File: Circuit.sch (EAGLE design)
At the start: 114 parts, among them IC1 LM1117T-3.3-V

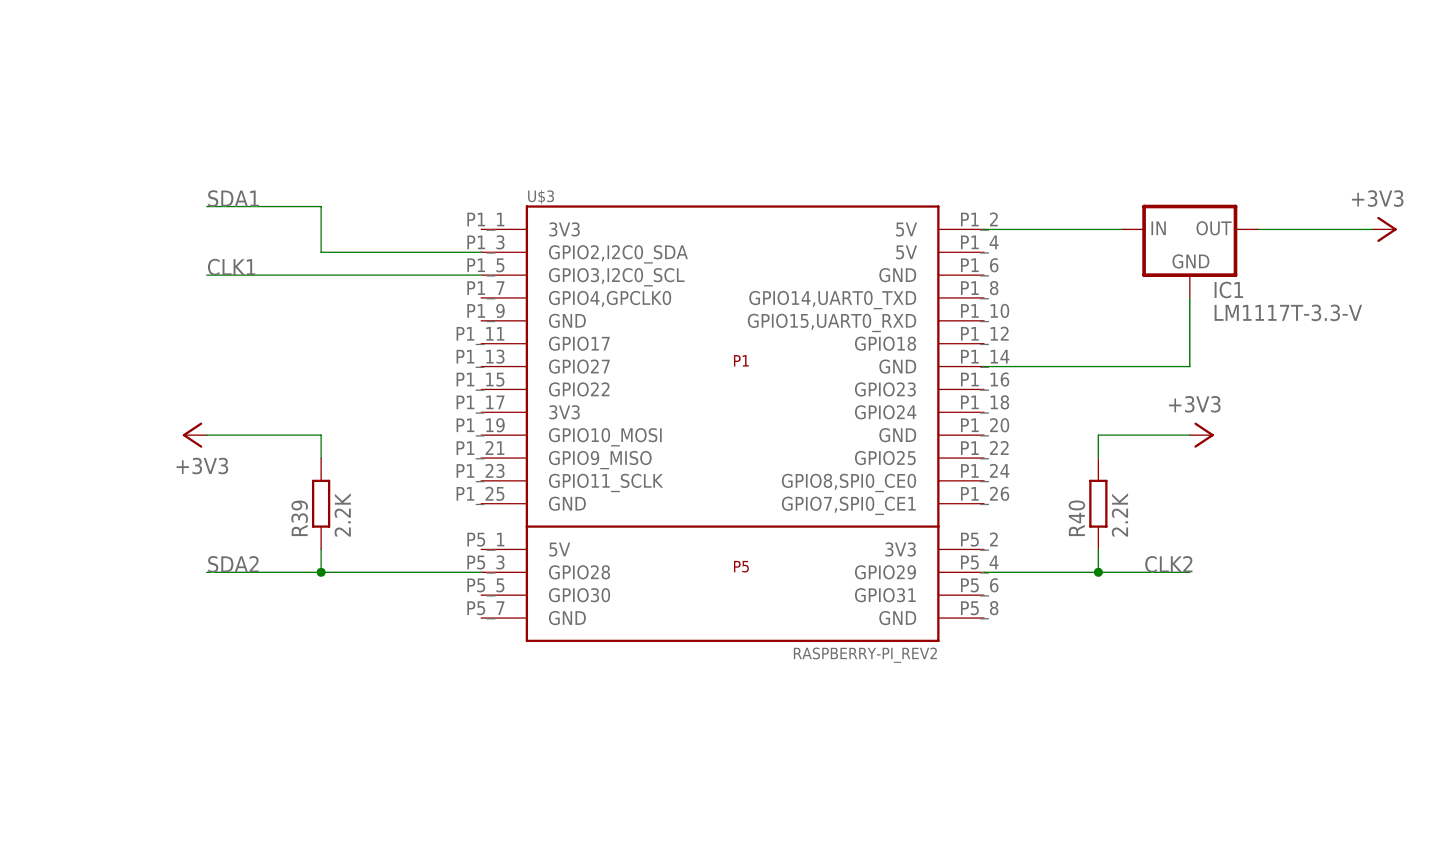
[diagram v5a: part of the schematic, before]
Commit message: Changed to smashed raspi headers
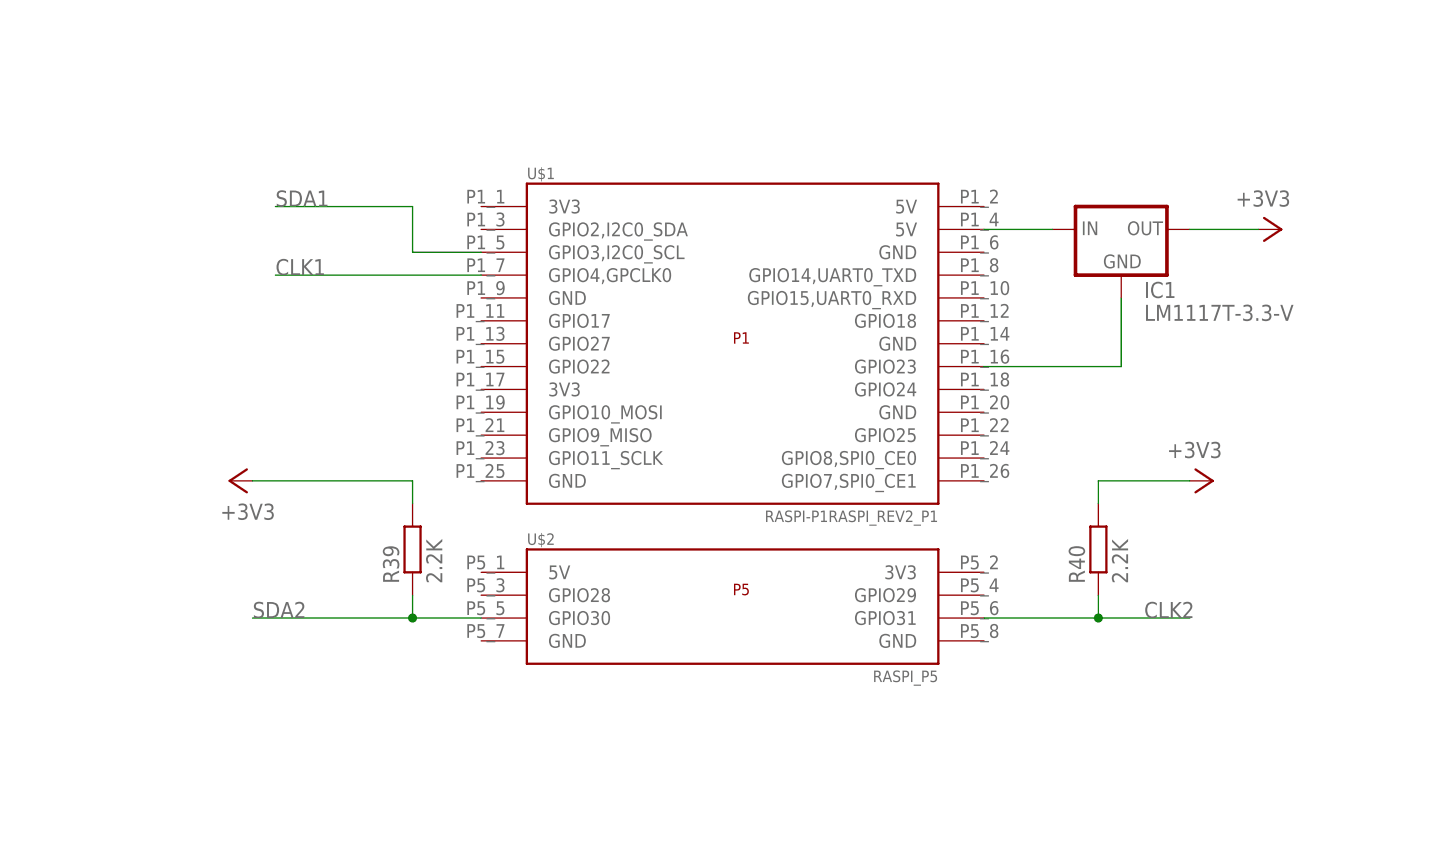
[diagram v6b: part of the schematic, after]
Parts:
- removed U$3: RASPBERRY-PI_REV2, RaspberryPi:RASPBERRY-PI_REV2
- added U$1: RASPI-P1RASPI_REV2_P1, Gyros:RASPI-P1RASPI_REV2_P1
- added U$2: RASPI_P5, RaspberryPi:RASPI_P5
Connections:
- net CLK1: now also U$1.GPIO4,GPCLK0; no longer U$3.GPIO3,I2C0_SCL
- net CLK2: now also U$2.GPIO31; no longer U$3.GPIO29
- net GND: now also U$1.GPIO23; no longer U$3.GND@14
- net N$10: now also U$1.5V@4; no longer U$3.5V@2
- net SDA1: now also U$1.GPIO3,I2C0_SCL; no longer U$3.GPIO2,I2C0_SDA
- net SDA2: now also U$2.GPIO30; no longer U$3.GPIO28
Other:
- moved on the sheet: IC1, R39, R40
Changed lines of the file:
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@@
 </classes>
 <parts>
-<part name="U$3" library="RaspberryPi" deviceset="RASPBERRY-PI_REV2" device=""/>
 <part name="MPU1" library="Gyros" deviceset="MPU-3300" device=""/>
 <part name="ITG1" library="Gyros" deviceset="ITG-3050" device=""/>
@@
 <part name="+3V51" library="supply1" deviceset="+3V3" device=""/>
 <part name="+3V31" library="supply1" deviceset="+3V3" device=""/>
+<part name="U$1" library="Gyros" deviceset="RASPI-P1" device="RASPI_REV2_P1"/>
+<part name="U$2" library="RaspberryPi" deviceset="RASPI_P5" device=""/>
 </parts>
 <sheets>
@@
 </plain>
 <instances>
-<instance part="U$3" gate="G$1" x="421.64" y="177.8"/>
 <instance part="MPU1" gate="G$1" x="-58.42" y="317.5"/>
 <instance part="ITG1" gate="G$1" x="-50.8" y="226.06"/>
@@
 <instance part="R9" gate="G$1" x="-22.86" y="345.44" rot="R180"/>
 <instance part="+3V46" gate="G$1" x="-5.08" y="350.52" rot="R270"/>
-<instance part="IC1" gate="G$1" x="472.44" y="193.04"/>
-<instance part="+3V5" gate="G$1" x="495.3" y="193.04" rot="R270"/>
-<instance part="R39" gate="G$1" x="375.92" y="162.56" rot="R90"/>
-<instance part="R40" gate="G$1" x="462.28" y="162.56" rot="R90"/>
-<instance part="+3V47" gate="G$1" x="474.98" y="170.18" rot="R270"/>
-<instance part="+3V48" gate="G$1" x="360.68" y="170.18" rot="R90"/>
+<instance part="IC1" gate="G$1" x="464.82" y="193.04"/>
+<instance part="+3V5" gate="G$1" x="482.6" y="193.04" rot="R270"/>
+<instance part="R39" gate="G$1" x="386.08" y="157.48" rot="R90"/>
+<instance part="R40" gate="G$1" x="462.28" y="157.48" rot="R90"/>
+<instance part="+3V47" gate="G$1" x="474.98" y="165.1" rot="R270"/>
+<instance part="+3V48" gate="G$1" x="365.76" y="165.1" rot="R90"/>
 <instance part="R23" gate="G$1" x="198.12" y="350.52" rot="R180"/>
 <instance part="R28" gate="G$1" x="215.9" y="345.44" rot="R180"/>
@@
 <instance part="+3V51" gate="G$1" x="246.38" y="160.02" rot="R270"/>
 <instance part="+3V31" gate="G$1" x="208.28" y="119.38" rot="R270"/>
+<instance part="U$1" gate="G$1" x="421.64" y="180.34"/>
+<instance part="U$2" gate="G$1" x="421.64" y="152.4"/>
 </instances>
 <busses>
@@
 <segment>
 <pinref part="IC1" gate="G$1" pin="GND"/>
-<wire x1="472.44" y1="185.42" x2="472.44" y2="177.8" width="0.1524" layer="91"/>
-<pinref part="U$3" gate="G$1" pin="GND@14"/>
-<wire x1="472.44" y1="177.8" x2="449.58" y2="177.8" width="0.1524" layer="91"/>
+<wire x1="464.82" y1="185.42" x2="464.82" y2="177.8" width="0.1524" layer="91"/>
+<wire x1="464.82" y1="177.8" x2="449.58" y2="177.8" width="0.1524" layer="91"/>
+<pinref part="U$1" gate="G$1" pin="GPIO23"/>
 </segment>
 </net>
 <net name="CLK1" class="0">
 <segment>
-<pinref part="U$3" gate="G$1" pin="GPIO3,I2C0_SCL"/>
-<wire x1="393.7" y1="187.96" x2="363.22" y2="187.96" width="0.1524" layer="91"/>
-<label x="363.22" y="187.96" size="1.778" layer="95"/>
+<wire x1="393.7" y1="187.96" x2="370.84" y2="187.96" width="0.1524" layer="91"/>
+<label x="370.84" y="187.96" size="1.778" layer="95"/>
+<pinref part="U$1" gate="G$1" pin="GPIO4,GPCLK0"/>
 </segment>
 <segment>
@@
 <net name="SDA1" class="0">
 <segment>
-<pinref part="U$3" gate="G$1" pin="GPIO2,I2C0_SDA"/>
-<wire x1="393.7" y1="190.5" x2="375.92" y2="190.5" width="0.1524" layer="91"/>
-<wire x1="375.92" y1="190.5" x2="375.92" y2="195.58" width="0.1524" layer="91"/>
-<wire x1="375.92" y1="195.58" x2="363.22" y2="195.58" width="0.1524" layer="91"/>
-<label x="363.22" y="195.58" size="1.778" layer="95"/>
+<wire x1="393.7" y1="190.5" x2="386.08" y2="190.5" width="0.1524" layer="91"/>
+<wire x1="386.08" y1="190.5" x2="386.08" y2="195.58" width="0.1524" layer="91"/>
+<wire x1="386.08" y1="195.58" x2="370.84" y2="195.58" width="0.1524" layer="91"/>
+<label x="370.84" y="195.58" size="1.778" layer="95"/>
+<pinref part="U$1" gate="G$1" pin="GPIO3,I2C0_SCL"/>
 </segment>
 <segment>
@@
 <net name="SDA2" class="0">
 <segment>
-<pinref part="U$3" gate="G$1" pin="GPIO28"/>
-<wire x1="393.7" y1="154.94" x2="375.92" y2="154.94" width="0.1524" layer="91"/>
-<label x="363.22" y="154.94" size="1.778" layer="95"/>
+<wire x1="393.7" y1="149.86" x2="386.08" y2="149.86" width="0.1524" layer="91"/>
+<label x="368.3" y="149.86" size="1.778" layer="95"/>
 <pinref part="R39" gate="G$1" pin="1"/>
-<wire x1="375.92" y1="154.94" x2="363.22" y2="154.94" width="0.1524" layer="91"/>
-<wire x1="375.92" y1="154.94" x2="375.92" y2="157.48" width="0.1524" layer="91"/>
-<junction x="375.92" y="154.94"/>
+<wire x1="386.08" y1="149.86" x2="368.3" y2="149.86" width="0.1524" layer="91"/>
+<wire x1="386.08" y1="149.86" x2="386.08" y2="152.4" width="0.1524" layer="91"/>
+<junction x="386.08" y="149.86"/>
+<pinref part="U$2" gate="G$1" pin="GPIO30"/>
 </segment>
 <segment>
@@
 <segment>
 <pinref part="IC1" gate="G$1" pin="OUT"/>
-<wire x1="480.06" y1="193.04" x2="492.76" y2="193.04" width="0.1524" layer="91"/>
+<wire x1="472.44" y1="193.04" x2="480.06" y2="193.04" width="0.1524" layer="91"/>
 <pinref part="+3V5" gate="G$1" pin="+3V3"/>
 </segment>
 <segment>
 <pinref part="R40" gate="G$1" pin="2"/>
-<wire x1="462.28" y1="167.64" x2="462.28" y2="170.18" width="0.1524" layer="91"/>
-<wire x1="462.28" y1="170.18" x2="472.44" y2="170.18" width="0.1524" layer="91"/>
+<wire x1="462.28" y1="162.56" x2="462.28" y2="165.1" width="0.1524" layer="91"/>
+<wire x1="462.28" y1="165.1" x2="472.44" y2="165.1" width="0.1524" layer="91"/>
 <pinref part="+3V47" gate="G$1" pin="+3V3"/>
 </segment>
 <segment>
 <pinref part="R39" gate="G$1" pin="2"/>
-<wire x1="375.92" y1="167.64" x2="375.92" y2="170.18" width="0.1524" layer="91"/>
-<wire x1="375.92" y1="170.18" x2="363.22" y2="170.18" width="0.1524" layer="91"/>
+<wire x1="386.08" y1="162.56" x2="386.08" y2="165.1" width="0.1524" layer="91"/>
+<wire x1="386.08" y1="165.1" x2="368.3" y2="165.1" width="0.1524" layer="91"/>
 <pinref part="+3V48" gate="G$1" pin="+3V3"/>
 </segment>
@@
 </segment>
 <segment>
-<pinref part="U$3" gate="G$1" pin="GPIO29"/>
-<wire x1="449.58" y1="154.94" x2="462.28" y2="154.94" width="0.1524" layer="91"/>
-<label x="467.36" y="154.94" size="1.778" layer="95"/>
+<wire x1="449.58" y1="149.86" x2="462.28" y2="149.86" width="0.1524" layer="91"/>
+<label x="467.36" y="149.86" size="1.778" layer="95"/>
 <pinref part="R40" gate="G$1" pin="1"/>
-<wire x1="462.28" y1="154.94" x2="472.44" y2="154.94" width="0.1524" layer="91"/>
-<wire x1="462.28" y1="154.94" x2="462.28" y2="157.48" width="0.1524" layer="91"/>
-<junction x="462.28" y="154.94"/>
+<wire x1="462.28" y1="149.86" x2="472.44" y2="149.86" width="0.1524" layer="91"/>
+<wire x1="462.28" y1="149.86" x2="462.28" y2="152.4" width="0.1524" layer="91"/>
+<junction x="462.28" y="149.86"/>
+<pinref part="U$2" gate="G$1" pin="GPIO31"/>
 </segment>
 </net>
@@
 <net name="N$10" class="0">
 <segment>
-<pinref part="U$3" gate="G$1" pin="5V@2"/>
 <pinref part="IC1" gate="G$1" pin="IN"/>
-<wire x1="449.58" y1="193.04" x2="464.82" y2="193.04" width="0.1524" layer="91"/>
-</segment>
-</net>
+<wire x1="449.58" y1="193.04" x2="457.2" y2="193.04" width="0.1524" layer="91"/>
+<pinref part="U$1" gate="G$1" pin="5V@4"/>
+</segment>
+</net>

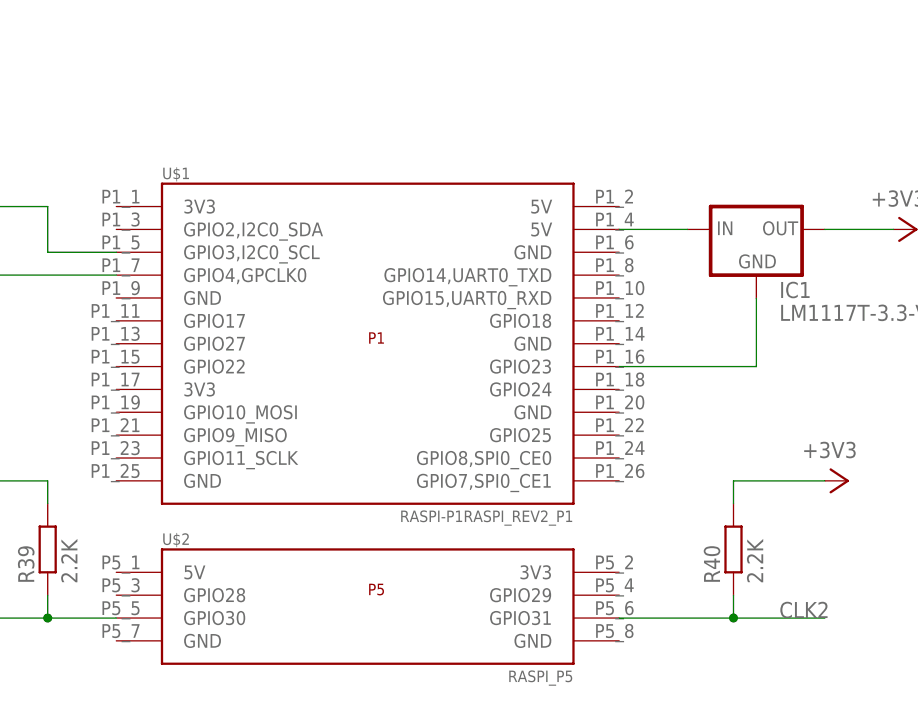
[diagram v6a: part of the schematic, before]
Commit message: Prior to removal of interupt wires
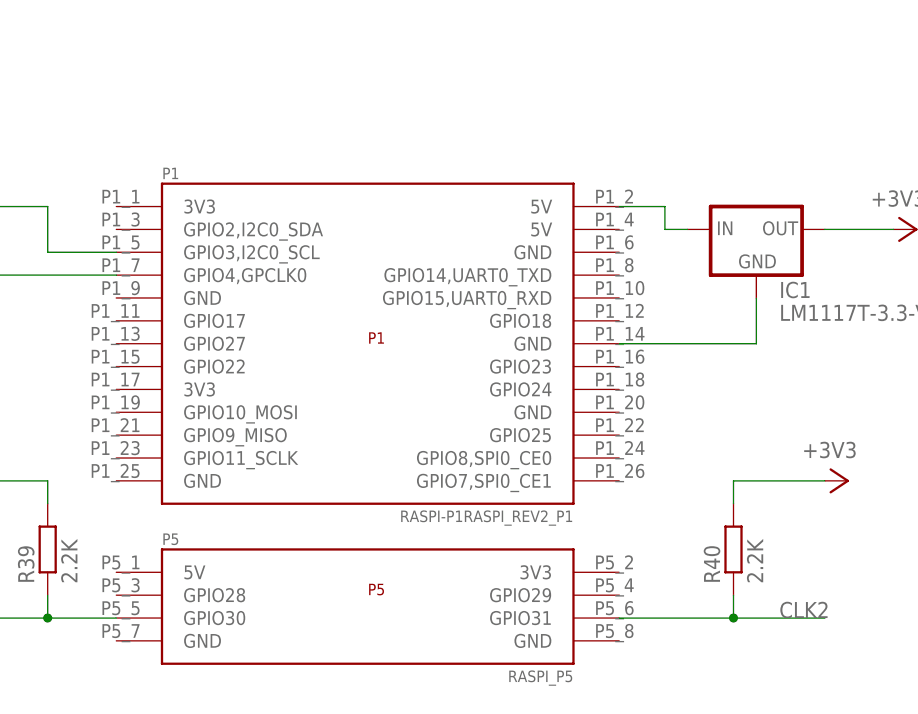
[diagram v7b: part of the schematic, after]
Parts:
- renumbered U$1 to P1, U$2 to P5
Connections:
- net GND: now also P1.GND@14; no longer P1.GPIO23
- net N$10: now also P1.5V@2; no longer P1.5V@4
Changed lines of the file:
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@@
 <part name="+3V51" library="supply1" deviceset="+3V3" device=""/>
 <part name="+3V31" library="supply1" deviceset="+3V3" device=""/>
-<part name="U$1" library="Gyros" deviceset="RASPI-P1" device="RASPI_REV2_P1"/>
-<part name="U$2" library="RaspberryPi" deviceset="RASPI_P5" device=""/>
+<part name="P1" library="Gyros" deviceset="RASPI-P1" device="RASPI_REV2_P1"/>
+<part name="P5" library="RaspberryPi" deviceset="RASPI_P5" device=""/>
 </parts>
 <sheets>
@@
 <instance part="+3V51" gate="G$1" x="246.38" y="160.02" rot="R270"/>
 <instance part="+3V31" gate="G$1" x="208.28" y="119.38" rot="R270"/>
-<instance part="U$1" gate="G$1" x="421.64" y="180.34"/>
-<instance part="U$2" gate="G$1" x="421.64" y="152.4"/>
+<instance part="P1" gate="G$1" x="421.64" y="180.34"/>
+<instance part="P5" gate="G$1" x="421.64" y="152.4"/>
 </instances>
 <busses>
@@
 <segment>
 <pinref part="IC1" gate="G$1" pin="GND"/>
-<wire x1="464.82" y1="185.42" x2="464.82" y2="177.8" width="0.1524" layer="91"/>
-<wire x1="464.82" y1="177.8" x2="449.58" y2="177.8" width="0.1524" layer="91"/>
-<pinref part="U$1" gate="G$1" pin="GPIO23"/>
+<wire x1="464.82" y1="185.42" x2="464.82" y2="180.34" width="0.1524" layer="91"/>
+<pinref part="P1" gate="G$1" pin="GND@14"/>
+<wire x1="464.82" y1="180.34" x2="449.58" y2="180.34" width="0.1524" layer="91"/>
 </segment>
 </net>
@@
 <wire x1="393.7" y1="187.96" x2="370.84" y2="187.96" width="0.1524" layer="91"/>
 <label x="370.84" y="187.96" size="1.778" layer="95"/>
-<pinref part="U$1" gate="G$1" pin="GPIO4,GPCLK0"/>
+<pinref part="P1" gate="G$1" pin="GPIO4,GPCLK0"/>
 </segment>
 <segment>
@@
 <wire x1="386.08" y1="195.58" x2="370.84" y2="195.58" width="0.1524" layer="91"/>
 <label x="370.84" y="195.58" size="1.778" layer="95"/>
-<pinref part="U$1" gate="G$1" pin="GPIO3,I2C0_SCL"/>
+<pinref part="P1" gate="G$1" pin="GPIO3,I2C0_SCL"/>
 </segment>
 <segment>
@@
 <wire x1="386.08" y1="149.86" x2="386.08" y2="152.4" width="0.1524" layer="91"/>
 <junction x="386.08" y="149.86"/>
-<pinref part="U$2" gate="G$1" pin="GPIO30"/>
+<pinref part="P5" gate="G$1" pin="GPIO30"/>
 </segment>
 <segment>
@@
 <wire x1="462.28" y1="149.86" x2="462.28" y2="152.4" width="0.1524" layer="91"/>
 <junction x="462.28" y="149.86"/>
-<pinref part="U$2" gate="G$1" pin="GPIO31"/>
+<pinref part="P5" gate="G$1" pin="GPIO31"/>
 </segment>
 </net>
@@
 <net name="N$10" class="0">
 <segment>
+<pinref part="P1" gate="G$1" pin="5V@2"/>
+<wire x1="449.58" y1="195.58" x2="454.66" y2="195.58" width="0.1524" layer="91"/>
+<wire x1="454.66" y1="195.58" x2="454.66" y2="193.04" width="0.1524" layer="91"/>
 <pinref part="IC1" gate="G$1" pin="IN"/>
-<wire x1="449.58" y1="193.04" x2="457.2" y2="193.04" width="0.1524" layer="91"/>
-<pinref part="U$1" gate="G$1" pin="5V@4"/>
-</segment>
-</net>
+<wire x1="454.66" y1="193.04" x2="457.2" y2="193.04" width="0.1524" layer="91"/>
+</segment>
+</net>
